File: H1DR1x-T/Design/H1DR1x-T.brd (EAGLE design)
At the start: 34.6 x 30 mm, 30 parts, among them P1 HEXABIT_17.32_NO_P6, P2 RS-485, U1 STM32G0B1CEU6QFN_B1CEU6_STM-L, U2 MAX14840EASAT, X1 XTALL_CSTCE8M00G52

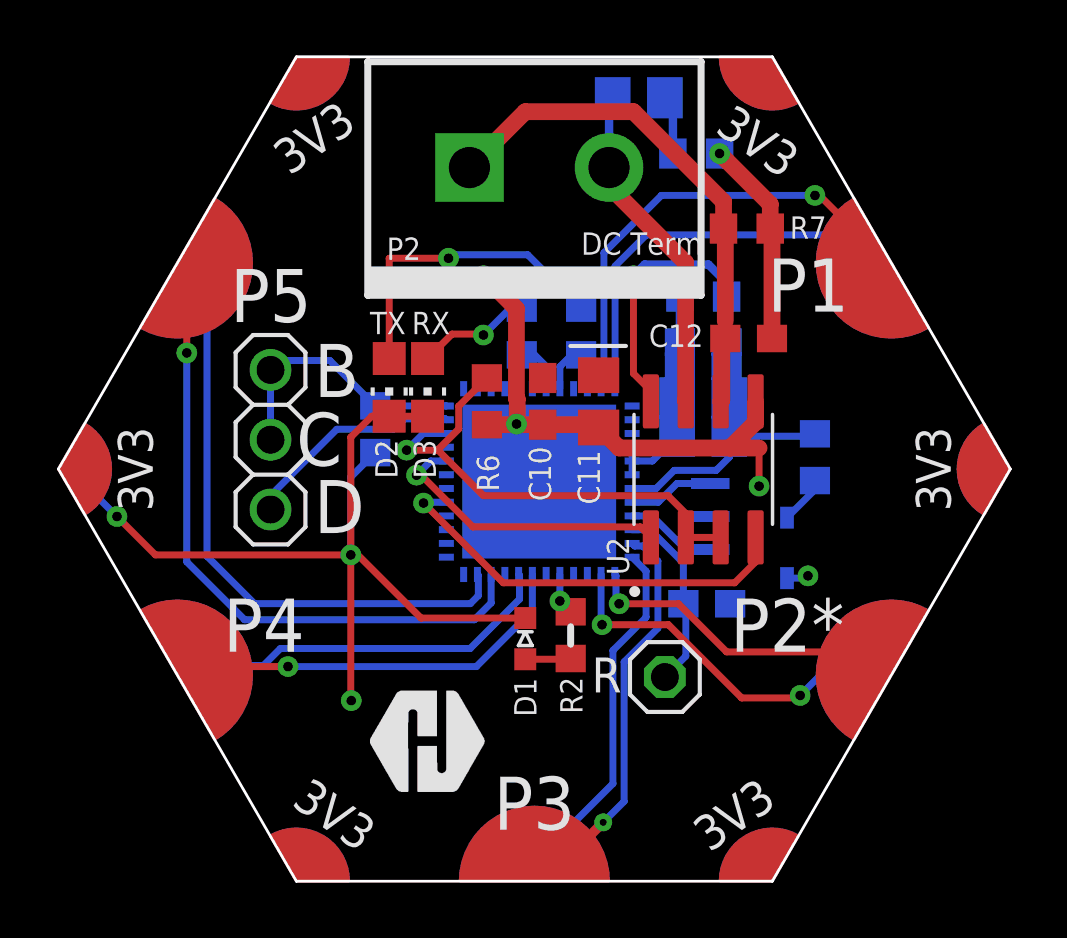
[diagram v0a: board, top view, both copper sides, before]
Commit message: - Fixed issues in PCB. - Regenerated output files.
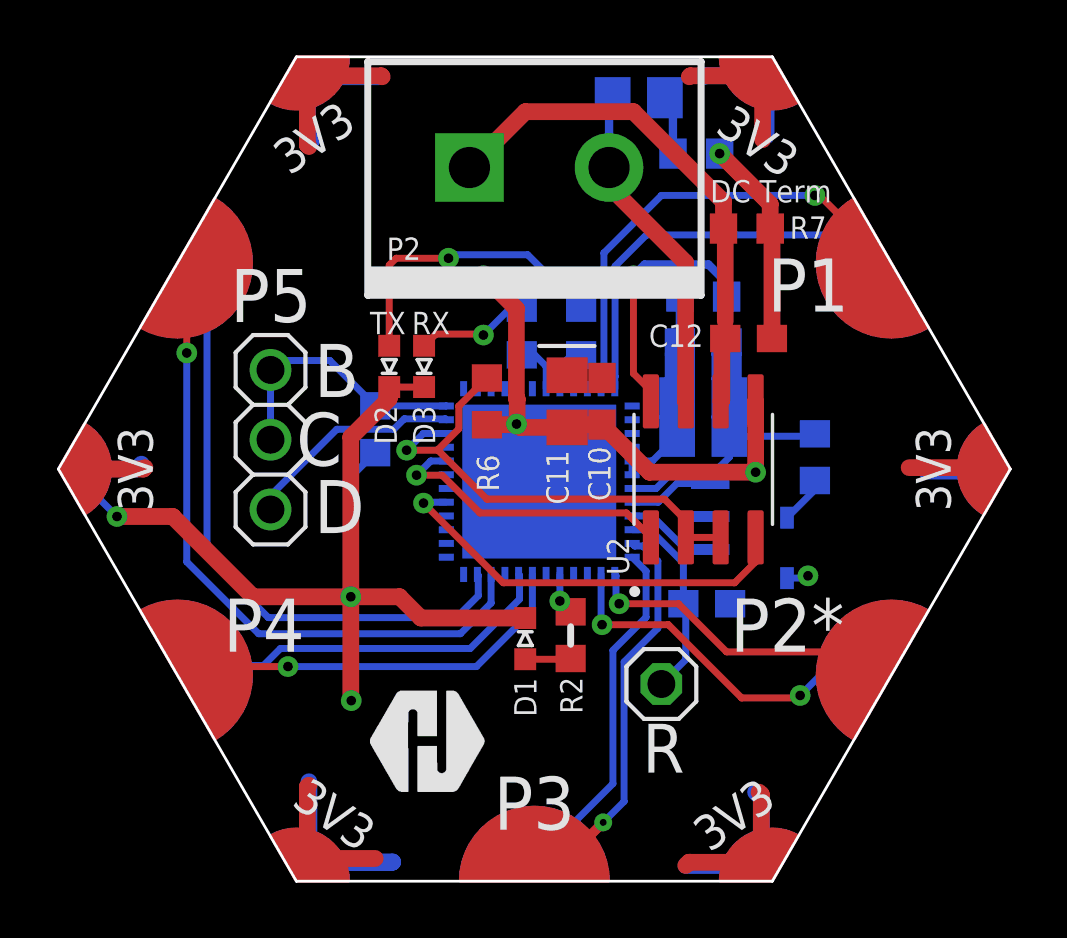
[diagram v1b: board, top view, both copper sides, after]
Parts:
- D2: value Yellow -> YELLOW; device HEXABITZ_USER_INTERFACE_PARTS:CHIP-LED0805 -> HEXABITZ_USER_INTERFACE_PARTS:VLMS1300-GS08
- D3: value Orange -> ORANGE; device HEXABITZ_USER_INTERFACE_PARTS:CHIP-LED0805 -> HEXABITZ_USER_INTERFACE_PARTS:VLMS1300-GS08
- moved C10 2.16 mm to (2.54, 17.5)
- moved C11 1.14 mm to (1.27, 17.5)
- moved D3 0.77 mm to (-3.94, 18.8), turned to 0 degrees
- moved D2 0.76 mm to (-5.21, 18.8), turned to 0 degrees
- moved R 0.28 mm to (4.70, 7.24), turned to 90 degrees
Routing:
- net GND: track 56.9 -> 87.8 mm
- net VDD: track 10.2 -> 36.6 mm
- net N$9: track 1.75 -> 0.95 mm
- net N$13: track 11.5 -> 10.9 mm
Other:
- board text added: "AC Term"
- board text added: "H1DR11"
- board text removed: "H1DR10"

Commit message: Everything is finished. I fixed some issues and reviewed everything.
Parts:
- removed C1: 1uF, HEXABITZ_RCLS:C-0805
- added C2: 1uF, HEXABITZ_RCLS:C-0805
- C10, C12: device Hexabitz:C-0603 -> HEXABITZ_RCLS:C-0603
- C11: device Hexabitz:C-0805-POL -> HEXABITZ_RCLS:C-0805-POL
- P2: device Hexabitz:1546111-2 -> HEXABITZ_CONNECTION_PARTS:1546111-2
- R1: value 0.0R -> 270R
- R2: value 270R -> 0.0R
- R4, R6, R7: device Hexabitz:R-0603 -> HEXABITZ_RCLS:R-0603
- R5: device Hexabitz:R-0805 -> HEXABITZ_RCLS:R-0603
- R8, R9: value 270.0R -> 270R
- U2: value MAX14840EASAT -> MAX14840EASA+T; device Hexabitz:SOIC127P600X175-8N -> HEXABITZ_ICs:SOIC127P600X175-8N
- moved R1 18.4 mm to (-3.81, 3.65), turned to 0 degrees
- moved R9 15.6 mm to (-5.08, 5.24), turned to 0 degrees
- moved R8 14.2 mm to (-5.40, 7.78)
- moved D3 12.9 mm to (0.48, 6.67), turned to 90 degrees
- moved D2 11.8 mm to (0.48, 8.41), turned to 90 degrees
- moved C12 11.1 mm to (-2.54, 23.7), flipped to the bottom, turned to 180 degrees
- moved R7 10.4 mm to (-2.54, 22.7), flipped to the bottom, turned to 0 degrees
- moved R2 9.29 mm to (6.67, 16.7), flipped to the bottom
- moved R 8.77 mm to (11.4, 12.9)
- moved C5 7.70 mm to (5.71, 11.1)
- moved D5 7.66 mm to (5.56, 18.9), turned to 0 degrees
- moved C6 7.64 mm to (5.71, 12.1)
- moved C3 7.18 mm to (11.4, 15.2), turned to 90 degrees
- moved R4 6.49 mm to (0.16, 23.7), turned to 0 degrees
- moved D1 6.44 mm to (-5.56, 5.24), turned to 90 degrees
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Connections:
- net N$7 renamed TB
- net N$8 renamed TA
- removed net N$11: R9.2, U1.43
- removed net N$9: R8.2, U1.44
- removed net UART1_RTS: R6.1, U1.34, U2.2, U2.3
- removed net UART1_RX: U1.32, U2.1
- removed net UART1_TX: U1.29, U2.4
- new net RX_LED: R9.2, U1.25
- new net TX_LED: R8.2, U1.26
- new net USART1_RX: P1.PAD_PD4, U1.32
- new net USART1_TX: P1.PAD_PU4, U1.29
- new net USART3_RTS: R6.1, U1.37, U2.2, U2.3
- net GND: now also R2.1; no longer R1.1
- net N$1: now also R1.2; no longer R2.2
- net N$3: now also R1.1; no longer R2.1
- net USART3_RX: now also U1.48, U2.1; no longer P1.PAD_PD5, U1.23
- net USART3_TX: now also U1.47, U2.4; no longer P1.PAD_PU5, U1.22
- net USART4_RX: now also P1.PAD_PD1; no longer P1.PAD_PD3
- net USART4_TX: now also P1.PAD_PU1; no longer P1.PAD_PU3
- net USART5_RX: now also P1.PAD_PD5, U1.40; no longer P1.PAD_PD4, U1.20
- net USART5_TX: now also P1.PAD_PU5, U1.41; no longer P1.PAD_PU4, U1.19
- net USART6_RX: now also P1.PAD_PD3, U1.16; no longer P1.PAD_PD1, U1.48
- net USART6_TX: now also P1.PAD_PU3, U1.15; no longer P1.PAD_PU1, U1.47
- net VDDA: now also C2.1; no longer C1.1
- net VSSA: now also C2.2, R2.2; no longer C1.2, R1.2
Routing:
- net VDD: track 36.6 -> 130.8 mm, vias 2 -> 1
- net GND: track 87.8 -> 50.3 mm, vias 6 -> 19
- net USART3_TX: track 24.3 -> 5.02 mm
- net UART1_RTS: track 18.2 -> 0.00 mm, vias 1 -> 0
- net USART3_RX: track 23.7 -> 6.24 mm, vias 0 -> 1
- net UART1_TX: track 15.3 -> 0.00 mm, vias 1 -> 0
- net USART6_TX: track 17.3 -> 5.78 mm
- net UART1_RX: track 10.8 -> 0.00 mm, vias 1 -> 0
- net USART4_RX: track 13.0 -> 23.8 mm
- net USART1_TX: track 0.00 -> 10.1 mm, vias 0 -> 1
- net USART1_RX: track 0.00 -> 9.85 mm
- net USART6_RX: track 15.0 -> 5.57 mm
- net USART4_TX: track 14.8 -> 22.8 mm
- net N$4: track 7.19 -> 13.4 mm
- net N$13: track 10.9 -> 5.29 mm
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- added copper zone on layer 1, net GND
- removed copper zone on layer 1, net VDD
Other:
- board text added: "*"
- board text added: "P4*"
- board text removed: "P4"
